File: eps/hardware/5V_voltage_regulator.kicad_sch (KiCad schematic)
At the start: 18 parts, among them U40 MP28167-A

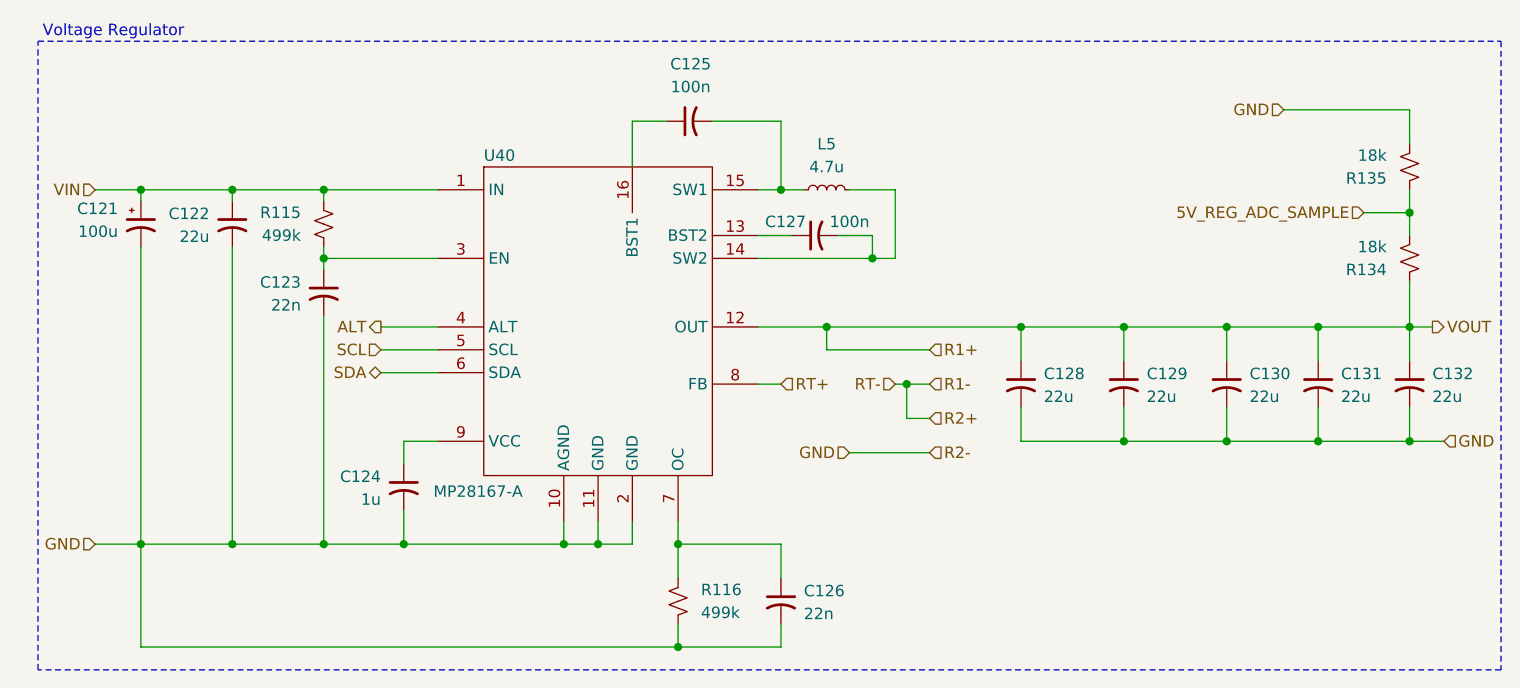
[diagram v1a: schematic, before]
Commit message: fix all ERC errors
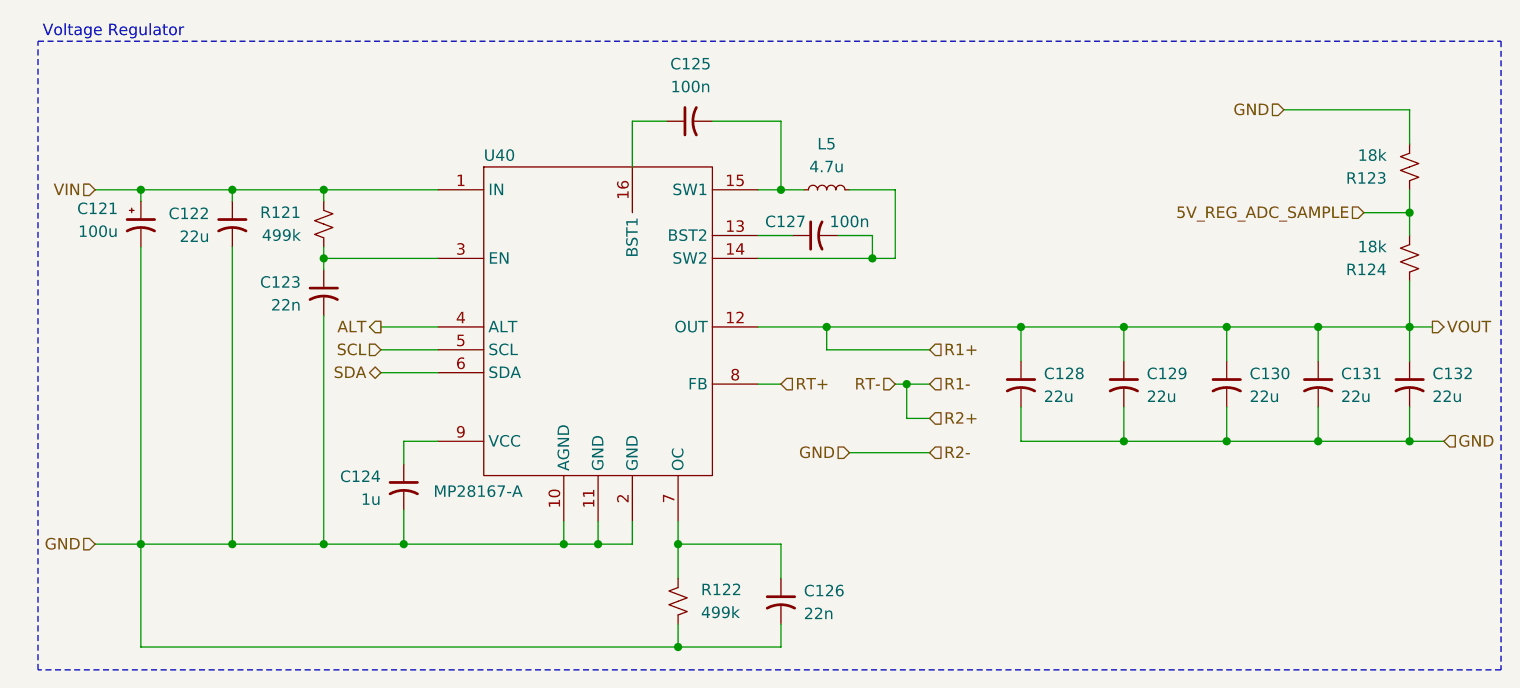
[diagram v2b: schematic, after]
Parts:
- renumbered R115 to R121, R116 to R122, R135 to R123, R134 to R124
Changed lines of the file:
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@@
 		(on_board yes)
 		(dnp no)
-		(property "Reference" "R135"
+		(property "Reference" "R123"
 			(at 228.6 74.9301 0)
 			(effects
@@
 			(project "eps"
 				(path "/9e0ae2e7-d4be-41b4-8312-0d2aceea2180/4806bc67-822a-440c-9458-e62de3f2a801"
-					(reference "R135")
+					(reference "R123")
 					(unit 1)
 				)
@@
 		(on_board yes)
 		(dnp no)
-		(property "Reference" "R116"
+		(property "Reference" "R122"
 			(at 152.4 120.6499 0)
 			(effects
@@
 			(project "eps"
 				(path "/9e0ae2e7-d4be-41b4-8312-0d2aceea2180/4806bc67-822a-440c-9458-e62de3f2a801"
-					(reference "R116")
+					(reference "R122")
 					(unit 1)
 				)
@@
 		(on_board yes)
 		(dnp no)
-		(property "Reference" "R134"
+		(property "Reference" "R124"
 			(at 228.6 85.0901 0)
 			(effects
@@
 			(project "eps"
 				(path "/9e0ae2e7-d4be-41b4-8312-0d2aceea2180/4806bc67-822a-440c-9458-e62de3f2a801"
-					(reference "R134")
+					(reference "R124")
 					(unit 1)
 				)
@@
 		(on_board yes)
 		(dnp no)
-		(property "Reference" "R115"
+		(property "Reference" "R121"
 			(at 107.95 78.7399 0)
 			(effects
@@
 				)
 				(path "/9e0ae2e7-d4be-41b4-8312-0d2aceea2180/4806bc67-822a-440c-9458-e62de3f2a801"
-					(reference "R115")
-					(unit 1)
-				)
+					(reference "R121")
+					(unit 1)
+				)

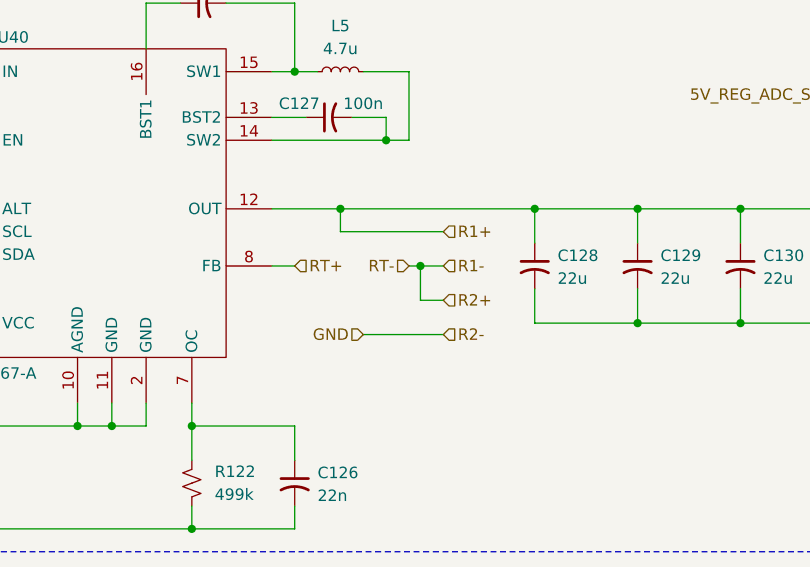
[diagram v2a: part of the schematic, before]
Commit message: fix all but one warning
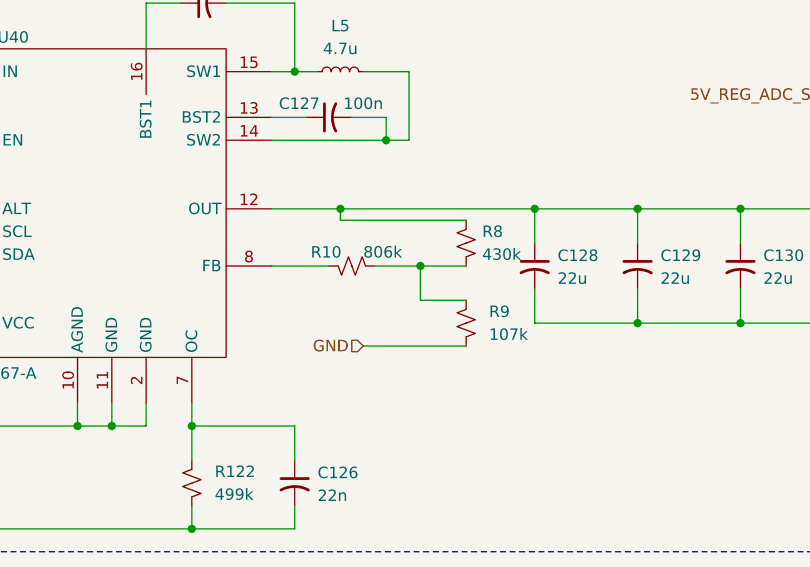
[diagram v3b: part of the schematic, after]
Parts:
- added R10: 806k, symbol Device:R_Small_US
- added R8: 430k, symbol Device:R_Small_US
- added R9: 107k, symbol Device:R_Small_US
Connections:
- net GND: now also R9.2
- net R1+ renamed VOUT
- net VOUT: now also R8.1
- net RT+: no longer names the net of U40.8 (FB)
- net RT+: now also R10.1
- new net: R10.2, R8.2, R9.1

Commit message: netlist fixes
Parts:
- renumbered R121 to R112, R122 to R113, R10 to R114, R8 to R115, R9 to R116, R123 to R117, R124 to R118
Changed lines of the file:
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@@
 		(on_board yes)
 		(dnp no)
-		(property "Reference" "R8"
+		(property "Reference" "R115"
 			(at 182.118 93.98 0)
 			(effects
@@
 			(project "eps"
 				(path "/9e0ae2e7-d4be-41b4-8312-0d2aceea2180/4806bc67-822a-440c-9458-e62de3f2a801"
-					(reference "R8")
+					(reference "R115")
 					(unit 1)
 				)
@@
 		(on_board yes)
 		(dnp no)
-		(property "Reference" "R10"
-			(at 163.068 96.266 90)
+		(property "Reference" "R114"
+			(at 161.544 96.266 90)
 			(effects
 				(font
@@
 			(project "eps"
 				(path "/9e0ae2e7-d4be-41b4-8312-0d2aceea2180/4806bc67-822a-440c-9458-e62de3f2a801"
-					(reference "R10")
+					(reference "R114")
 					(unit 1)
 				)
@@
 		(on_board yes)
 		(dnp no)
-		(property "Reference" "R123"
+		(property "Reference" "R117"
 			(at 228.6 74.9301 0)
 			(effects
@@
 			(project "eps"
 				(path "/9e0ae2e7-d4be-41b4-8312-0d2aceea2180/4806bc67-822a-440c-9458-e62de3f2a801"
-					(reference "R123")
+					(reference "R117")
 					(unit 1)
 				)
@@
 		(on_board yes)
 		(dnp no)
-		(property "Reference" "R9"
+		(property "Reference" "R116"
 			(at 182.88 102.8699 0)
 			(effects
@@
 			(project "eps"
 				(path "/9e0ae2e7-d4be-41b4-8312-0d2aceea2180/4806bc67-822a-440c-9458-e62de3f2a801"
-					(reference "R9")
+					(reference "R116")
 					(unit 1)
 				)
@@
 		(on_board yes)
 		(dnp no)
-		(property "Reference" "R122"
+		(property "Reference" "R113"
 			(at 152.4 120.6499 0)
 			(effects
@@
 			(project "eps"
 				(path "/9e0ae2e7-d4be-41b4-8312-0d2aceea2180/4806bc67-822a-440c-9458-e62de3f2a801"
-					(reference "R122")
+					(reference "R113")
 					(unit 1)
 				)
@@
 		(on_board yes)
 		(dnp no)
-		(property "Reference" "R124"
+		(property "Reference" "R118"
 			(at 228.6 85.0901 0)
 			(effects
@@
 			(project "eps"
 				(path "/9e0ae2e7-d4be-41b4-8312-0d2aceea2180/4806bc67-822a-440c-9458-e62de3f2a801"
-					(reference "R124")
+					(reference "R118")
 					(unit 1)
 				)
@@
 		(on_board yes)
 		(dnp no)
-		(property "Reference" "R121"
+		(property "Reference" "R112"
 			(at 107.95 78.7399 0)
 			(effects
@@
 				)
 				(path "/9e0ae2e7-d4be-41b4-8312-0d2aceea2180/4806bc67-822a-440c-9458-e62de3f2a801"
-					(reference "R121")
-					(unit 1)
-				)
+					(reference "R112")
+					(unit 1)
+				)

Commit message: start footprint assignment
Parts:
- C121: footprint (none) -> Capacitor_Tantalum_SMD:CP_EIA-3216-18_Kemet-A
- C122, C123, C124, C125, C126, C127, C128, C129, C130, C131, C132: footprint (none) -> Capacitor_SMD:C_0603_1608Metric
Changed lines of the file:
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@@
 			)
 		)
-		(property "Footprint" ""
+		(property "Footprint" "Capacitor_SMD:C_0603_1608Metric"
 			(at 119.38 109.22 0)
 			(effects
@@
 			)
 		)
-		(property "Footprint" ""
+		(property "Footprint" "Capacitor_SMD:C_0603_1608Metric"
 			(at 100.33 80.01 0)
 			(effects
@@
 			)
 		)
-		(property "Footprint" ""
+		(property "Footprint" "Capacitor_SMD:C_0603_1608Metric"
 			(at 220.98 97.79 0)
 			(effects
@@
 			)
 		)
-		(property "Footprint" ""
+		(property "Footprint" "Capacitor_SMD:C_0603_1608Metric"
 			(at 199.39 97.79 0)
 			(effects
@@
 			)
 		)
-		(property "Footprint" ""
+		(property "Footprint" "Capacitor_SMD:C_0603_1608Metric"
 			(at 165.1 81.28 0)
 			(effects
@@
 			)
 		)
-		(property "Footprint" ""
+		(property "Footprint" "Capacitor_SMD:C_0603_1608Metric"
 			(at 187.96 97.79 0)
 			(effects
@@
 			)
 		)
-		(property "Footprint" ""
+		(property "Footprint" "Capacitor_SMD:C_0603_1608Metric"
 			(at 210.82 97.79 0)
 			(effects
@@
 			)
 		)
-		(property "Footprint" ""
+		(property "Footprint" "Capacitor_Tantalum_SMD:CP_EIA-3216-18_Kemet-A"
 			(at 90.17 80.01 0)
 			(effects
@@
 			)
 		)
-		(property "Footprint" ""
+		(property "Footprint" "Capacitor_SMD:C_0603_1608Metric"
 			(at 231.14 97.79 0)
 			(effects
@@
 			)
 		)
-		(property "Footprint" ""
+		(property "Footprint" "Capacitor_SMD:C_0603_1608Metric"
 			(at 161.29 121.92 0)
 			(effects
@@
 			)
 		)
-		(property "Footprint" ""
+		(property "Footprint" "Capacitor_SMD:C_0603_1608Metric"
 			(at 151.13 68.58 0)
 			(effects
@@
 			)
 		)
-		(property "Footprint" ""
+		(property "Footprint" "Capacitor_SMD:C_0603_1608Metric"
 			(at 110.49 87.63 0)
 			(effects

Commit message: finish footprint assignment and board setup
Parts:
- L5: footprint (none) -> Inductor_SMD:L_Vishay_IHLP-2020
- R112, R113, R114, R115, R116, R117, R118: footprint (none) -> Resistor_SMD:R_0603_1608Metric
- U40: footprint (none) -> Package_DFN_QFN:MPS_QFN-16_3x3mm_P0.5mm
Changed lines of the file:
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@@
 			)
 		)
-		(property "Footprint" ""
+		(property "Footprint" "Resistor_SMD:R_0603_1608Metric"
 			(at 180.34 95.25 0)
 			(effects
@@
 			)
 		)
-		(property "Footprint" ""
+		(property "Footprint" "Resistor_SMD:R_0603_1608Metric"
 			(at 167.64 97.79 0)
 			(effects
@@
 			)
 		)
-		(property "Footprint" ""
+		(property "Footprint" "Resistor_SMD:R_0603_1608Metric"
 			(at 231.14 73.66 0)
 			(effects
@@
 			)
 		)
-		(property "Footprint" ""
+		(property "Footprint" "Package_DFN_QFN:MPS_QFN-16_3x3mm_P0.5mm"
 			(at 140.97 91.44 0)
 			(effects
@@
 			)
 		)
-		(property "Footprint" ""
+		(property "Footprint" "Resistor_SMD:R_0603_1608Metric"
 			(at 180.34 104.14 0)
 			(effects
@@
 			)
 		)
-		(property "Footprint" ""
+		(property "Footprint" "Inductor_SMD:L_Vishay_IHLP-2020"
 			(at 166.37 76.2 0)
 			(effects
@@
 			)
 		)
-		(property "Footprint" ""
+		(property "Footprint" "Resistor_SMD:R_0603_1608Metric"
 			(at 149.86 121.92 0)
 			(effects
@@
 			)
 		)
-		(property "Footprint" ""
+		(property "Footprint" "Resistor_SMD:R_0603_1608Metric"
 			(at 231.14 83.82 0)
 			(effects
@@
 			)
 		)
-		(property "Footprint" ""
+		(property "Footprint" "Resistor_SMD:R_0603_1608Metric"
 			(at 110.49 80.01 0)
 			(effects

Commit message: schematic fixes
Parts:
- C122, C123, C124, C125, C126, C127, C128, C129, C130, C131, C132: footprint Capacitor_SMD:C_0603_1608Metric -> Capacitor_SMD:C_0402_1005Metric
- R112, R113, R114, R115, R116, R117, R118: footprint Resistor_SMD:R_0603_1608Metric -> Resistor_SMD:R_0402_1005Metric
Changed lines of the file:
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@@
 			)
 		)
-		(property "Footprint" "Resistor_SMD:R_0603_1608Metric"
+		(property "Footprint" "Resistor_SMD:R_0402_1005Metric"
 			(at 180.34 95.25 0)
 			(effects
@@
 			)
 		)
-		(property "Footprint" "Capacitor_SMD:C_0603_1608Metric"
+		(property "Footprint" "Capacitor_SMD:C_0402_1005Metric"
 			(at 119.38 109.22 0)
 			(effects
@@
 			)
 		)
-		(property "Footprint" "Capacitor_SMD:C_0603_1608Metric"
+		(property "Footprint" "Capacitor_SMD:C_0402_1005Metric"
 			(at 100.33 80.01 0)
 			(effects
@@
 			)
 		)
-		(property "Footprint" "Resistor_SMD:R_0603_1608Metric"
+		(property "Footprint" "Resistor_SMD:R_0402_1005Metric"
 			(at 167.64 97.79 0)
 			(effects
@@
 			)
 		)
-		(property "Footprint" "Resistor_SMD:R_0603_1608Metric"
+		(property "Footprint" "Resistor_SMD:R_0402_1005Metric"
 			(at 231.14 73.66 0)
 			(effects
@@
 			)
 		)
-		(property "Footprint" "Capacitor_SMD:C_0603_1608Metric"
+		(property "Footprint" "Capacitor_SMD:C_0402_1005Metric"
 			(at 220.98 97.79 0)
 			(effects
@@
 			)
 		)
-		(property "Footprint" "Resistor_SMD:R_0603_1608Metric"
+		(property "Footprint" "Resistor_SMD:R_0402_1005Metric"
 			(at 180.34 104.14 0)
 			(effects
@@
 			)
 		)
-		(property "Footprint" "Capacitor_SMD:C_0603_1608Metric"
+		(property "Footprint" "Capacitor_SMD:C_0402_1005Metric"
 			(at 199.39 97.79 0)
 			(effects
@@
 			)
 		)
-		(property "Footprint" "Capacitor_SMD:C_0603_1608Metric"
+		(property "Footprint" "Capacitor_SMD:C_0402_1005Metric"
 			(at 165.1 81.28 0)
 			(effects
@@
 			)
 		)
-		(property "Footprint" "Resistor_SMD:R_0603_1608Metric"
+		(property "Footprint" "Resistor_SMD:R_0402_1005Metric"
 			(at 149.86 121.92 0)
 			(effects
@@
 			)
 		)
-		(property "Footprint" "Capacitor_SMD:C_0603_1608Metric"
+		(property "Footprint" "Capacitor_SMD:C_0402_1005Metric"
 			(at 187.96 97.79 0)
 			(effects
@@
 			)
 		)
-		(property "Footprint" "Capacitor_SMD:C_0603_1608Metric"
+		(property "Footprint" "Capacitor_SMD:C_0402_1005Metric"
 			(at 210.82 97.79 0)
 			(effects
@@
 			)
 		)
-		(property "Footprint" "Capacitor_SMD:C_0603_1608Metric"
+		(property "Footprint" "Capacitor_SMD:C_0402_1005Metric"
 			(at 231.14 97.79 0)
 			(effects
@@
 			)
 		)
-		(property "Footprint" "Resistor_SMD:R_0603_1608Metric"
+		(property "Footprint" "Resistor_SMD:R_0402_1005Metric"
 			(at 231.14 83.82 0)
 			(effects
@@
 			)
 		)
-		(property "Footprint" "Capacitor_SMD:C_0603_1608Metric"
+		(property "Footprint" "Capacitor_SMD:C_0402_1005Metric"
 			(at 161.29 121.92 0)
 			(effects
@@
 			)
 		)
-		(property "Footprint" "Capacitor_SMD:C_0603_1608Metric"
+		(property "Footprint" "Capacitor_SMD:C_0402_1005Metric"
 			(at 151.13 68.58 0)
 			(effects
@@
 			)
 		)
-		(property "Footprint" "Resistor_SMD:R_0603_1608Metric"
+		(property "Footprint" "Resistor_SMD:R_0402_1005Metric"
 			(at 110.49 80.01 0)
 			(effects
@@
 			)
 		)
-		(property "Footprint" "Capacitor_SMD:C_0603_1608Metric"
+		(property "Footprint" "Capacitor_SMD:C_0402_1005Metric"
 			(at 110.49 87.63 0)
 			(effects

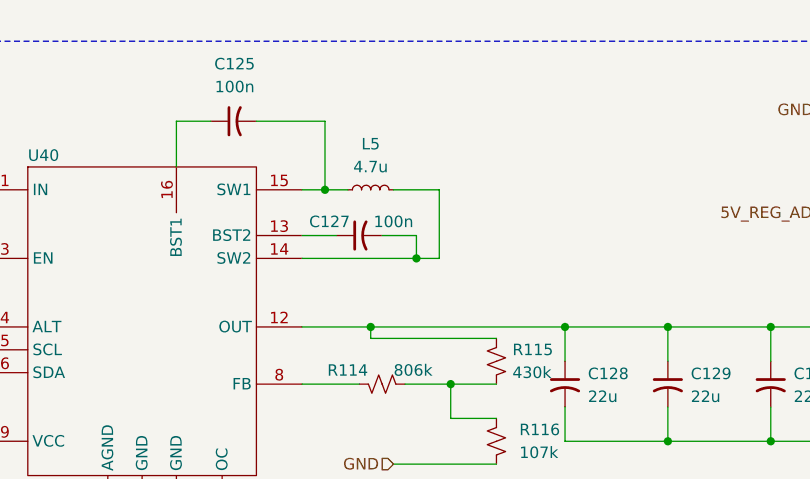
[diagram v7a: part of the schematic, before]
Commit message: finish component placement
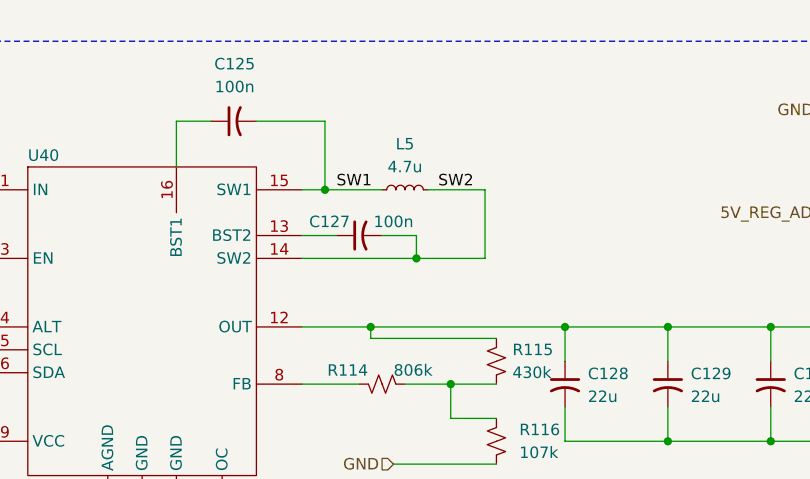
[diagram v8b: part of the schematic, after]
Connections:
- net SW2: now reaches C127.2, L5.2, U40.14 (SW2)
- net SW1: now reaches C125.2, L5.1, U40.15 (SW1)
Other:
- moved on the sheet: L5
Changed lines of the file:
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@@
 	(wire
 		(pts
-			(xy 173.99 76.2) (xy 173.99 83.82)
+			(xy 179.07 76.2) (xy 179.07 83.82)
 		)
 		(stroke
@@
 	(wire
 		(pts
-			(xy 161.29 76.2) (xy 163.83 76.2)
+			(xy 161.29 76.2) (xy 167.64 76.2)
 		)
 		(stroke
@@
 	(wire
 		(pts
-			(xy 173.99 83.82) (xy 171.45 83.82)
+			(xy 179.07 83.82) (xy 171.45 83.82)
 		)
 		(stroke
@@
 	(wire
 		(pts
-			(xy 168.91 76.2) (xy 173.99 76.2)
+			(xy 172.72 76.2) (xy 179.07 76.2)
 		)
 		(stroke
@@
 			(width 0)
 			(type default)
+		)
+	)
+	(label "SW2"
+		(at 177.8 76.2 180)
+		(effects
+			(font
+				(size 1.27 1.27)
+			)
+			(justify right bottom)
+		)
+	)
+	(label "SW1"
+		(at 162.56 76.2 0)
+		(effects
+			(font
+				(size 1.27 1.27)
+			)
+			(justify left bottom)
 		)
 	)
@@
 	(symbol
 		(lib_id "Device:L_Small")
-		(at 166.37 76.2 90)
+		(at 170.18 76.2 90)
 		(unit 1)
 		(exclude_from_sim no)
@@
 		(fields_autoplaced yes)
 		(property "Reference" "L5"
-			(at 166.37 71.12 90)
+			(at 170.18 71.12 90)
 			(effects
 				(font
@@
 		)
 		(property "Value" "4.7u"
-			(at 166.37 73.66 90)
+			(at 170.18 73.66 90)
 			(effects
 				(font
@@
 		)
 		(property "Footprint" "Inductor_SMD:L_Vishay_IHLP-2020"
-			(at 166.37 76.2 0)
+			(at 170.18 76.2 0)
 			(effects
 				(font
@@
 		)
 		(property "Datasheet" "~"
-			(at 166.37 76.2 0)
+			(at 170.18 76.2 0)
 			(effects
 				(font
@@
 		)
 		(property "Description" "Inductor, small symbol"
-			(at 166.37 76.2 0)
-			(effects
-				(font
+			(at 170.18 76.2 0)
+			(effects
+				(font
